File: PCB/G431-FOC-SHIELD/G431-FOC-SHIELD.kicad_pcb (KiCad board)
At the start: 4 copper layers, 80 x 95 mm, 34 parts, among them CN10 Conn_02x19_Odd_Even, CN7 Conn_02x19_Odd_Even, J1 Screw_Terminal_01x02, J2 Screw_Terminal_01x03, Q1 Q_NMOS_GDS, Q2 Q_NMOS_GDS, Q3 Q_NMOS_GDS, Q4 Q_NMOS_GDS, Q5 Q_NMOS_GDS, Q6 Q_NMOS_GDS, U1 DRV8323RSRGZR

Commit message: redoing layout
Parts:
- removed C1: 100n, Capacitor_SMD:C_0603_1608Metric
- removed C10, C11, C9: 4.7u, Capacitor_SMD:C_1210_3225Metric
- removed C12: 4700u, Capacitor_THT:CP_Radial_D16.0mm_P7.50mm
- removed C2: 2.2u, Capacitor_SMD:C_0805_2012Metric
- removed C3: 10u, Capacitor_SMD:C_0805_2012Metric
- removed C4: 47n, Capacitor_SMD:C_0805_2012Metric
- removed C5, C7, C8: 1u, Capacitor_SMD:C_0603_1608Metric
- removed C6: 0.1u, Capacitor_SMD:C_0603_1608Metric
- removed CN10, CN7: Conn_02x19_Odd_Even, Connector_PinSocket_2.54mm:PinSocket_2x19_P2.54mm_Vertical
- removed D1: D_Schottky, Diode_SMD:D_SMA
- removed J1: Screw_Terminal_01x02, TerminalBlock_Phoenix:TerminalBlock_Phoenix_MKDS-1,5-2_1x02_P5.00mm_Horizontal
- removed J2: Screw_Terminal_01x03, TerminalBlock_Phoenix:TerminalBlock_Phoenix_MKDS-1,5-3_1x03_P5.00mm_Horizontal
- removed L1: 22uH, Inductor_SMD:L_1210_3225Metric
- removed Q1, Q2, Q3, Q4, Q5, Q6: Q_NMOS_GDS, Package_TO_SOT_SMD:TO-263-3_TabPin2
- removed R1, R3, R8: 100k, Resistor_SMD:R_0603_1608Metric
- removed R2: 331.4k, Resistor_SMD:R_0603_1608Metric
- removed R4, R9: 10k, Resistor_SMD:R_0603_1608Metric
- removed R5, R6, R7: 2m, Resistor_SMD:R_2512_6332Metric
- removed U1: DRV8323RSRGZR, DRV8323RSRGZR:QFN50P700X700X100-49N
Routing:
- removed copper zone on In1.Cu, net GND
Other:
- board size 80 x 95 mm -> 70 x 70 mm
- board text removed: "FOC-SHIELD"
- board text removed: "®©®"

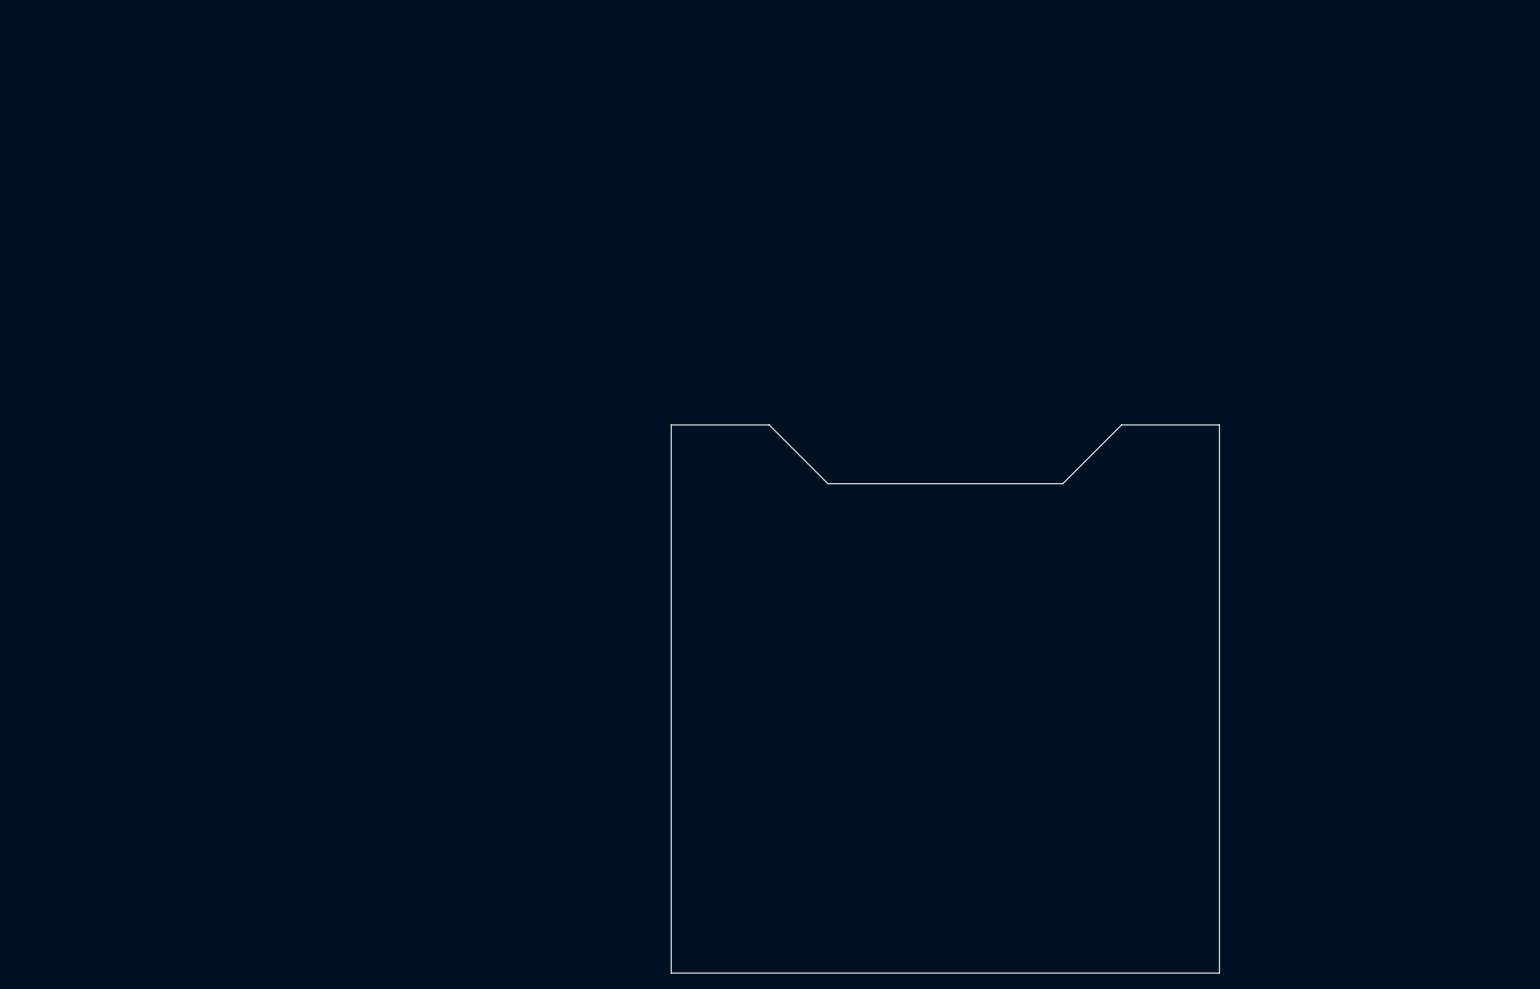
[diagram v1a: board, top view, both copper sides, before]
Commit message: using custom cad for edge, placement started
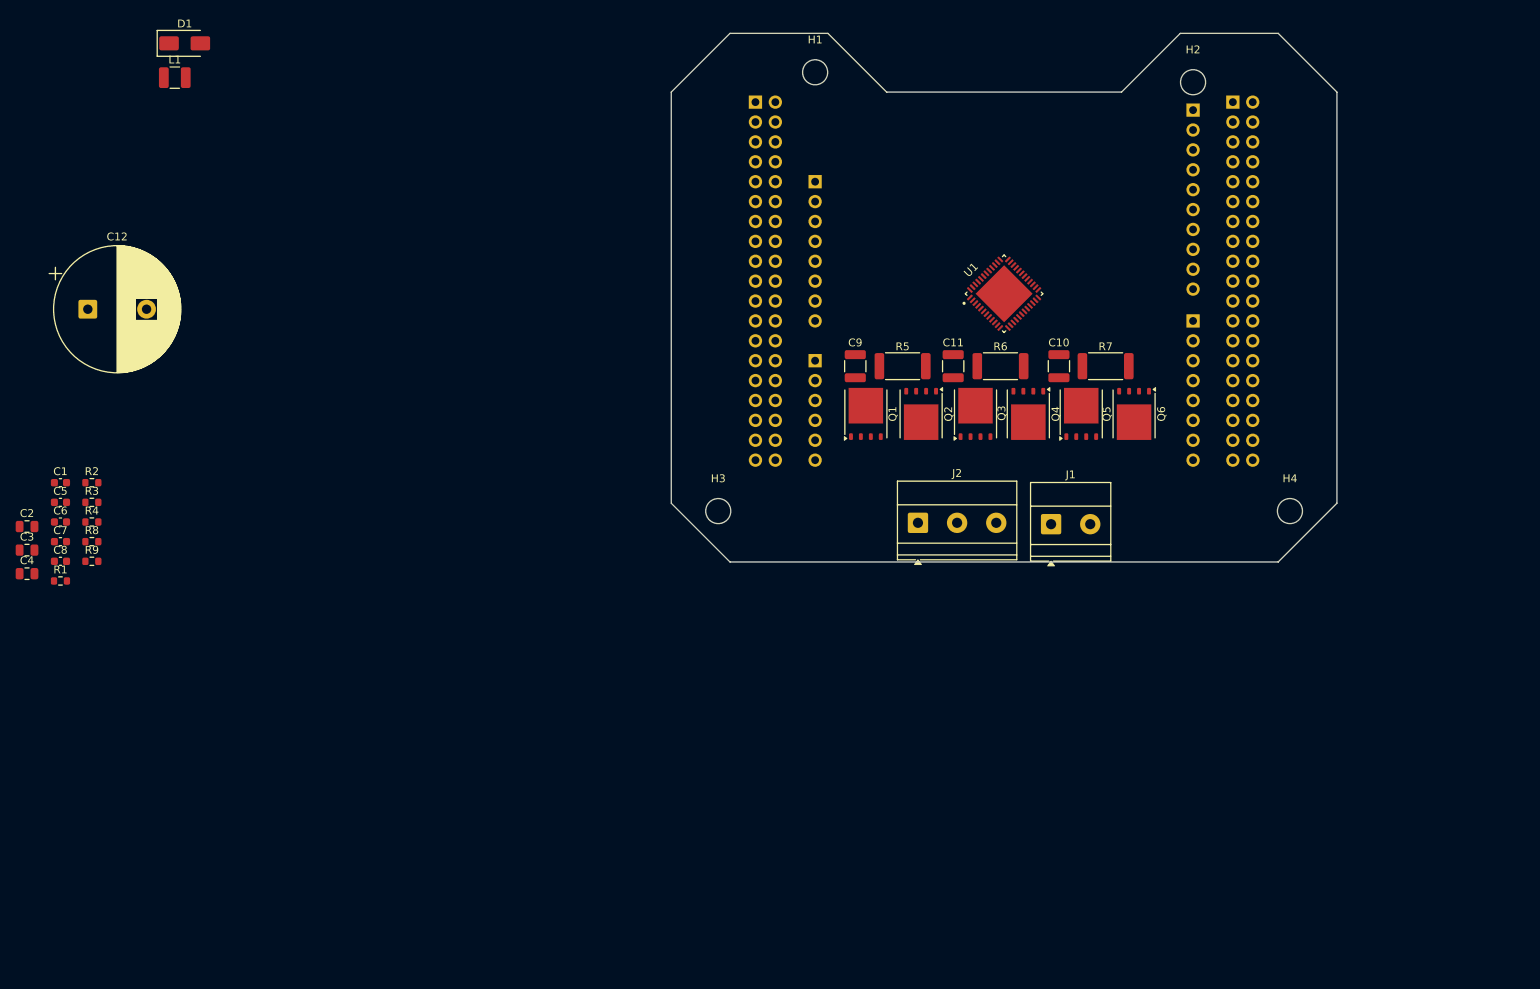
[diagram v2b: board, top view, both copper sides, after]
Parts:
- added C1: 100n, Capacitor_SMD:C_0603_1608Metric, F.Cu at (52.0, 77.4)
- added C10: 4.7u, Capacitor_SMD:C_1210_3225Metric, F.Cu at (179.5, 62.5)
- added C11: 4.7u, Capacitor_SMD:C_1210_3225Metric, F.Cu at (166.0, 62.5)
- added C12: 4700u, Capacitor_THT:CP_Radial_D16.0mm_P7.50mm, F.Cu at (55.5, 55.2)
- added C2: 2.2u, Capacitor_SMD:C_0805_2012Metric, F.Cu at (47.7, 83.0)
- added C3: 10u, Capacitor_SMD:C_0805_2012Metric, F.Cu at (47.7, 86.0)
- added C4: 47n, Capacitor_SMD:C_0805_2012Metric, F.Cu at (47.7, 89.0)
- added C5: 1u, Capacitor_SMD:C_0603_1608Metric, F.Cu at (52.0, 79.9)
- added C6: 0.1u, Capacitor_SMD:C_0603_1608Metric, F.Cu at (52.0, 82.4)
- added C7: 1u, Capacitor_SMD:C_0603_1608Metric, F.Cu at (52.0, 84.9)
- added C8: 1u, Capacitor_SMD:C_0603_1608Metric, F.Cu at (52.0, 87.4)
- added C9: 4.7u, Capacitor_SMD:C_1210_3225Metric, F.Cu at (153.5, 62.5)
- added CN10: Conn_02x19_Odd_Even, Connector_PinSocket_2.54mm:PinSocket_2x19_P2.54mm_Vertical, B.Cu at (201.7, 28.8)
- added CN7: Conn_02x19_Odd_Even, Connector_PinSocket_2.54mm:PinSocket_2x19_P2.54mm_Vertical, B.Cu at (140.8, 28.8)
- added D1: D_Schottky, Diode_SMD:D_SMA, F.Cu at (67.9, 21.3)
- added H1: MountingHole, MountingHole:MountingHole_3.2mm_M3, F.Cu at (148.4, 25.0)
- added H2: MountingHole, MountingHole:MountingHole_3.2mm_M3, F.Cu at (196.6, 26.2)
- added H3: MountingHole, MountingHole:MountingHole_3.2mm_M3, F.Cu at (136.0, 81.0)
- added H4: MountingHole, MountingHole:MountingHole_3.2mm_M3, F.Cu at (209.0, 81.0)
- added J1: Screw_Terminal_01x02, TerminalBlock_Phoenix:TerminalBlock_Phoenix_MKDS-1,5-2_1x02_P5.00mm_Horizontal, F.Cu at (178.5, 82.7)
- added J2: Screw_Terminal_01x03, TerminalBlock_Phoenix:TerminalBlock_Phoenix_MKDS-1,5-3_1x03_P5.00mm_Horizontal, F.Cu at (161.5, 82.5)
- added J3: Conn_01x06, Connector_PinHeader_2.54mm:PinHeader_1x06_P2.54mm_Vertical, B.Cu at (148.4, 61.8)
- added J4: Conn_01x08, Connector_PinHeader_2.54mm:PinHeader_1x08_P2.54mm_Vertical, B.Cu at (148.4, 38.9)
- added J5: Conn_01x08, Connector_PinHeader_2.54mm:PinHeader_1x08_P2.54mm_Vertical, B.Cu at (196.6, 56.7)
- added J6: Conn_01x10, Connector_PinHeader_2.54mm:PinHeader_1x10_P2.54mm_Vertical, B.Cu at (196.6, 29.8)
- added L1: 22uH, Inductor_SMD:L_1210_3225Metric, F.Cu at (66.6, 25.7)
- added Q1: BSC070N10NS3G, Package_TO_SOT_SMD:TDSON-8-1, F.Cu at (154.8, 68.6)
- added Q2: BSC070N10NS3G, Package_TO_SOT_SMD:TDSON-8-1, F.Cu at (161.9, 68.6)
- added Q3: BSC070N10NS3G, Package_TO_SOT_SMD:TDSON-8-1, F.Cu at (168.8, 68.6)
- added Q4: BSC070N10NS3G, Package_TO_SOT_SMD:TDSON-8-1, F.Cu at (175.6, 68.6)
- added Q5: BSC070N10NS3G, Package_TO_SOT_SMD:TDSON-8-1, F.Cu at (182.3, 68.6)
- added Q6: BSC070N10NS3G, Package_TO_SOT_SMD:TDSON-8-1, F.Cu at (189.1, 68.6)
- added R1: 100k, Resistor_SMD:R_0603_1608Metric, F.Cu at (52.0, 89.9)
- added R2: 331.4k, Resistor_SMD:R_0603_1608Metric, F.Cu at (56.0, 77.4)
- added R3: 100k, Resistor_SMD:R_0603_1608Metric, F.Cu at (56.0, 79.9)
- added R4: 10k, Resistor_SMD:R_0603_1608Metric, F.Cu at (56.0, 82.4)
- added R5: 2m, Resistor_SMD:R_2512_6332Metric, F.Cu at (159.5, 62.5)
- added R6: 2m, Resistor_SMD:R_2512_6332Metric, F.Cu at (172.0, 62.5)
- added R7: 2m, Resistor_SMD:R_2512_6332Metric, F.Cu at (185.5, 62.5)
- added R8: 100k, Resistor_SMD:R_0603_1608Metric, F.Cu at (56.0, 84.9)
- added R9: 10k, Resistor_SMD:R_0603_1608Metric, F.Cu at (56.0, 87.4)
- added U1: DRV8323RSRGZR, DRV8323RSRGZR:QFN50P700X700X100-49N, F.Cu at (172.5, 53.2)
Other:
- board size 70 x 70 mm -> 85 x 67.5 mm

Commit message: routed motor drive stuff, started header pin routing
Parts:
- moved C12 171.9 mm to (227.0, 66.5)
- moved C1 117.9 mm to (160.8, 32.0)
- moved C5 117.9 mm to (160.8, 34.5)
- moved C6 117.9 mm to (160.8, 37.0)
- moved C7 117.9 mm to (160.8, 39.5)
- moved C8 117.9 mm to (160.8, 42.0)
- moved R1 117.9 mm to (160.8, 44.5)
- moved C2 117.9 mm to (156.5, 37.6)
- moved C3 117.9 mm to (156.5, 40.6)
- moved C4 117.9 mm to (156.5, 43.6)
- moved R2 117.9 mm to (164.8, 32.0)
- moved R3 117.9 mm to (164.8, 34.5)
- moved R4 117.9 mm to (164.8, 37.0)
- moved R8 117.9 mm to (164.8, 39.5)
- moved R9 117.9 mm to (164.8, 42.0)
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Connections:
- J3 pad 1: /PA0 -> unconnected-(J3-Pin_1-Pad1)
- J3 pad 2: /PA1 -> unconnected-(J3-Pin_2-Pad2)
- J3 pad 3: /PA4 -> unconnected-(J3-Pin_3-Pad3)
- J3 pad 4: /PB0 -> unconnected-(J3-Pin_4-Pad4)
- J3 pad 5: /PC1/PB9 -> unconnected-(J3-Pin_5-Pad5)
- J3 pad 6: /PC0/PA15 -> unconnected-(J3-Pin_6-Pad6)
- J4 pad 1: /NC -> unconnected-(J4-Pin_1-Pad1)
- J4 pad 2: /IOREF -> unconnected-(J4-Pin_2-Pad2)
- J4 pad 3: /NRST -> unconnected-(J4-Pin_3-Pad3)
- J4 pad 4: /+3V3 -> unconnected-(J4-Pin_4-Pad4)
- J4 pad 5: /+5V -> unconnected-(J4-Pin_5-Pad5)
- J4 pad 6: GND -> unconnected-(J4-Pin_6-Pad6)
- J4 pad 7: GND -> unconnected-(J4-Pin_7-Pad7)
- J4 pad 8: /VIN -> unconnected-(J4-Pin_8-Pad8)
- J6 pad 1: /INHB -> unconnected-(J6-Pin_1-Pad1)
- J6 pad 10: /PB8 -> unconnected-(J6-Pin_10-Pad10)
- J6 pad 2: /PC7 -> unconnected-(J6-Pin_2-Pad2)
- J6 pad 3: /PB6 -> unconnected-(J6-Pin_3-Pad3)
- J6 pad 4: /PA7 -> unconnected-(J6-Pin_4-Pad4)
- J6 pad 5: /PA6 -> unconnected-(J6-Pin_5-Pad5)
- J6 pad 6: /PA5 -> unconnected-(J6-Pin_6-Pad6)
- J6 pad 7: GND -> unconnected-(J6-Pin_7-Pad7)
- J6 pad 8: /AVDD -> unconnected-(J6-Pin_8-Pad8)
- J6 pad 9: /PB9 -> unconnected-(J6-Pin_9-Pad9)
- U1 pad 24: /PC1 -> /PC1/PB9
- U1 pad 25: /PC0 -> /PC0/PA15
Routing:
- net VM: track 0.00 -> 80.3 mm, vias 0 -> 17
- net /INHC: track 0.00 -> 74.5 mm, vias 0 -> 1
- net /INHB: track 0.00 -> 71.8 mm
- net /INHA: track 0.00 -> 62.0 mm
- net /INLA: track 0.00 -> 58.9 mm, vias 0 -> 1
- net /ENABLE: track 0.00 -> 47.2 mm, vias 0 -> 1
- net /INLB: track 0.00 -> 41.7 mm, vias 0 -> 1
- net /INLC: track 0.00 -> 40.0 mm, vias 0 -> 1
- net /PA7: track 0.00 -> 34.6 mm
- net /PB12: track 0.00 -> 32.3 mm, vias 0 -> 1
- net /PA5: track 0.00 -> 30.8 mm
- net /PA6: track 0.00 -> 29.3 mm
- net /C: track 0.00 -> 26.9 mm
- net /GHA: track 0.00 -> 23.8 mm
- net /GHC: track 0.00 -> 23.6 mm
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- added copper zone on In1.Cu, net GND
- added copper zone on In2.Cu, net GND
- added copper zone on B.Cu, net VM
